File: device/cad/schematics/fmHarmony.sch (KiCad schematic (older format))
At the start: 18 parts, among them IC1 7805

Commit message: Station Log added to web app, with text-file-based physical device updates in mind. PCB and Schematic updated
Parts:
- removed U?: Ultimate_GPS_Breakout_V3, symbol Ultimate_GPS_Breakout_V3
- removed U?: Sheaff-Monk_Programmer, symbol Sheaff-Monk_Programmer
- added C7: 100n, ~, symbol C
- added IC3: ULTIMATE_GPS_BREAKOUT_V3, symbol ULTIMATE_GPS_BREAKOUT_V3
- added IC4: SHEAFF-MONK_SERIAL_TRANSLATOR, DIL32, symbol SHEAFF-MONK_SERIAL_TRANSLATOR
- added JP3: SHEAFF-MONK_PROGRAMMER, symbol SHEAFF-MONK_PROGRAMMER
- gave numbers to parts that had none: 2
- renumbered Rres to R1, Rback to R2, Rcon to VR1
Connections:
- wire segments 76 -> 100
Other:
- note removed: "GND"
- moved on the sheet: C4, C5, C6, IC2, LCD1, R1, R2, VR1

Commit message: PCB improved.
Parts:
- renumbered JP3 to JP2
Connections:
- net labels added: JP1
- net labels removed: Vin
- wire segments 100 -> 105
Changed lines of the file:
@@
 Sheet 1 1
 Title ""
-Date "27 sep 2014"
+Date "30 sep 2014"
 Rev ""
 Comp ""
@@
 L GND #PWR?
 U 1 1 5417678B
-P 8700 2100
-F 0 "#PWR?" H 8700 2100 30  0001 C CNN
-F 1 "GND" H 8700 2030 30  0001 C CNN
-F 2 "" H 8700 2100 60  0000 C CNN
-F 3 "" H 8700 2100 60  0000 C CNN
-	1    8700 2100
+P 8200 2100
+F 0 "#PWR?" H 8200 2100 30  0001 C CNN
+F 1 "GND" H 8200 2030 30  0001 C CNN
+F 2 "" H 8200 2100 60  0000 C CNN
+F 3 "" H 8200 2100 60  0000 C CNN
+	1    8200 2100
 	1    0    0    -1
 $EndComp
@@
 L VCC #PWR?
 U 1 1 5417679F
-P 8200 1900
-F 0 "#PWR?" H 8200 2000 30  0001 C CNN
-F 1 "VCC" H 8200 2000 30  0000 C CNN
-F 2 "" H 8200 1900 60  0000 C CNN
-F 3 "" H 8200 1900 60  0000 C CNN
-	1    8200 1900
+P 8700 1900
+F 0 "#PWR?" H 8700 2000 30  0001 C CNN
+F 1 "VCC" H 8700 2000 30  0000 C CNN
+F 2 "" H 8700 1900 60  0000 C CNN
+F 3 "" H 8700 1900 60  0000 C CNN
+	1    8700 1900
 	1    0    0    -1
 $EndComp
@@
 $EndComp
 Text GLabel 950  1350 0    60   Input ~ 0
-Vin
+JP1
 $Comp
 L GND #PWR?
@@
 $EndComp
 $Comp
-L SHEAFF-MONK_PROGRAMMER JP3
+L SHEAFF-MONK_PROGRAMMER JP2
 U 1 1 5426FD03
 P 4600 4600
-F 0 "JP3" V 4200 4950 60  0000 C CNN
+F 0 "JP2" V 4200 4950 60  0000 C CNN
 F 1 "SHEAFF-MONK_PROGRAMMER" H 4650 4500 60  0000 C CNN
 F 2 "" H 4650 4500 60  0000 C CNN
@@
 	9100 2400 8950 2400
 Wire Wire Line
-	8200 2000 8200 1900
-Wire Wire Line
-	8700 2000 8700 2100
+	8700 2000 8700 1900
+Wire Wire Line
+	8200 2000 8200 2100
 Wire Wire Line
 	6250 3900 5800 3900
@@
 Wire Wire Line
 	5900 4100 6250 4100
+$Comp
+L GND #PWR?
+U 1 1 5428D3A8
+P 8350 3550
+F 0 "#PWR?" H 8350 3550 30  0001 C CNN
+F 1 "GND" H 8350 3480 30  0001 C CNN
+F 2 "" H 8350 3550 60  0000 C CNN
+F 3 "" H 8350 3550 60  0000 C CNN
+	1    8350 3550
+	1    0    0    -1
+$EndComp
+Wire Wire Line
+	8250 3500 8350 3500
+Wire Wire Line
+	8350 3500 8350 3550
+Wire Wire Line
+	8250 3600 8300 3600
+Wire Wire Line
+	8300 3600 8300 3650
+Wire Wire Line
+	8300 3650 8450 3650
+Connection ~ 8450 3650
 $EndSCHEMATC

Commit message: PCB Updated to include jumper for separate car/update power sources
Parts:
- added JP4: JUMPER3, ~, symbol JUMPER3
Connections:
- wire segments 105 -> 113
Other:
- note added: "Car"
- note added: "Update"
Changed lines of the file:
@@
 Sheet 1 1
 Title ""
-Date "30 sep 2014"
+Date "1 oct 2014"
 Rev ""
 Comp ""
@@
 L VCC #PWR?
 U 1 1 5424B3C1
-P 5600 1150
-F 0 "#PWR?" H 5600 1250 30  0001 C CNN
-F 1 "VCC" H 5600 1250 30  0000 C CNN
-F 2 "" H 5600 1150 60  0000 C CNN
-F 3 "" H 5600 1150 60  0000 C CNN
-	1    5600 1150
+P 6650 1400
+F 0 "#PWR?" H 6650 1500 30  0001 C CNN
+F 1 "VCC" H 6650 1500 30  0000 C CNN
+F 2 "" H 6650 1400 60  0000 C CNN
+F 3 "" H 6650 1400 60  0000 C CNN
+	1    6650 1400
 	1    0    0    -1
 $EndComp
@@
 	1    0    0    -1
 $EndComp
-Text Notes 5700 1150 0    60   ~ 0
+Text Notes 6750 1400 0    60   ~ 0
 +5V\n
-$Comp
-L SHEAFF-MONK_SERIAL_TRANSLATOR IC4
-U 1 1 5426F555
-P 7200 7100
-F 0 "IC4" H 6400 9030 40  0000 L BNN
-F 1 "SHEAFF-MONK_SERIAL_TRANSLATOR" H 7100 6950 40  0000 L BNN
-F 2 "DIL32" H 7250 7200 30  0000 C CIN
-F 3 "" H 7250 7200 60  0000 C CNN
-	1    7200 7100
-	1    0    0    -1
-$EndComp
-$Comp
-L VCC #PWR?
-U 1 1 5426F80A
-P 5750 5500
-F 0 "#PWR?" H 5750 5600 30  0001 C CNN
-F 1 "VCC" H 5750 5600 30  0000 C CNN
-F 2 "" H 5750 5500 60  0000 C CNN
-F 3 "" H 5750 5500 60  0000 C CNN
-	1    5750 5500
-	1    0    0    -1
-$EndComp
 $Comp
 L GND #PWR?
@@
 Connection ~ 4000 1900
 Wire Wire Line
-	5100 1350 5600 1350
+	5100 1350 6200 1350
 Wire Wire Line
 	5250 1350 5250 1400
-Wire Wire Line
-	5600 1350 5600 1150
 Connection ~ 5250 1350
 Wire Wire Line
@@
 	8300 3650 8450 3650
 Connection ~ 8450 3650
+$Comp
+L JUMPER3 JP4
+U 1 1 542C4C4B
+P 6450 1050
+F 0 "JP4" H 6500 950 40  0000 L CNN
+F 1 "JUMPER3" H 6450 1150 40  0000 C CNN
+F 2 "~" H 6450 1050 60  0000 C CNN
+F 3 "~" H 6450 1050 60  0000 C CNN
+	1    6450 1050
+	1    0    0    -1
+$EndComp
+Wire Wire Line
+	6450 1150 6450 1400
+Wire Wire Line
+	6450 1400 6650 1400
+Wire Wire Line
+	6200 1350 6200 1050
+$Comp
+L SHEAFF-MONK_SERIAL_TRANSLATOR IC4
+U 1 1 5426F555
+P 7200 7100
+F 0 "IC4" H 6400 9030 40  0000 L BNN
+F 1 "SHEAFF-MONK_SERIAL_TRANSLATOR" H 7100 6950 40  0000 L BNN
+F 2 "DIL32" H 7250 7200 30  0000 C CIN
+F 3 "" H 7250 7200 60  0000 C CNN
+	1    7200 7100
+	1    0    0    -1
+$EndComp
+Wire Wire Line
+	5750 5500 5750 5300
+Wire Wire Line
+	5750 5300 6200 5300
+Wire Wire Line
+	6200 5300 6200 5100
+Wire Wire Line
+	6200 5100 10200 5100
+Wire Wire Line
+	10200 5100 10200 1050
+Wire Wire Line
+	10200 1050 6700 1050
+Text Notes 6050 950  0    60   ~ 0
+Car
+Text Notes 6700 950  0    60   ~ 0
+Update
 $EndSCHEMATC

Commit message: improved PCB and schematic. PCB sent in for fabrication Mk1
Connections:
- wire segments 113 -> 117
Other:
- note added: "JP3\n"
- moved on the sheet: C3
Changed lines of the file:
@@
 Sheet 1 1
 Title ""
-Date "1 oct 2014"
+Date "5 oct 2014"
 Rev ""
 Comp ""
@@
 L CP1 C3
 U 1 1 5424AA5D
-P 5250 1600
-F 0 "C3" H 5300 1700 50  0000 L CNN
-F 1 "1u" H 5300 1500 50  0000 L CNN
-F 2 "~" H 5250 1600 60  0000 C CNN
-F 3 "~" H 5250 1600 60  0000 C CNN
-	1    5250 1600
+P 6450 1600
+F 0 "C3" H 6500 1700 50  0000 L CNN
+F 1 "1u" H 6500 1500 50  0000 L CNN
+F 2 "~" H 6450 1600 60  0000 C CNN
+F 3 "~" H 6450 1600 60  0000 C CNN
+	1    6450 1600
 	1    0    0    -1
 $EndComp
@@
 Wire Wire Line
 	4400 1350 4600 1350
-Wire Wire Line
-	5250 1900 5250 1800
 Connection ~ 4000 1900
 Wire Wire Line
 	5100 1350 6200 1350
-Wire Wire Line
-	5250 1350 5250 1400
 Connection ~ 5250 1350
 Wire Wire Line
@@
 Text Notes 6700 950  0    60   ~ 0
 Update
+$Comp
+L GND #PWR?
+U 1 1 54316390
+P 6450 2000
+F 0 "#PWR?" H 6450 2000 30  0001 C CNN
+F 1 "GND" H 6450 1930 30  0001 C CNN
+F 2 "" H 6450 2000 60  0000 C CNN
+F 3 "" H 6450 2000 60  0000 C CNN
+	1    6450 2000
+	1    0    0    -1
+$EndComp
+Wire Wire Line
+	6450 1800 6450 2000
+Wire Wire Line
+	5700 2600 6250 2600
+Wire Wire Line
+	6250 2700 5700 2700
+Wire Wire Line
+	6250 2800 5700 2800
+Wire Wire Line
+	6250 2900 5700 2900
+Wire Wire Line
+	6250 3000 5700 3000
+Text Notes 5650 2850 1    60   ~ 0
+JP3\n
 $EndSCHEMATC

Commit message: updated project schematic
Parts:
- added LED1, LED2, LED3: (no value), ~, symbol LED
- added R3, R4, R5: 100, symbol R
- added SW1: (no value), ~, symbol SW_PUSH
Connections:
- wire segments 117 -> 131
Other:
- note removed: "JP3\n"

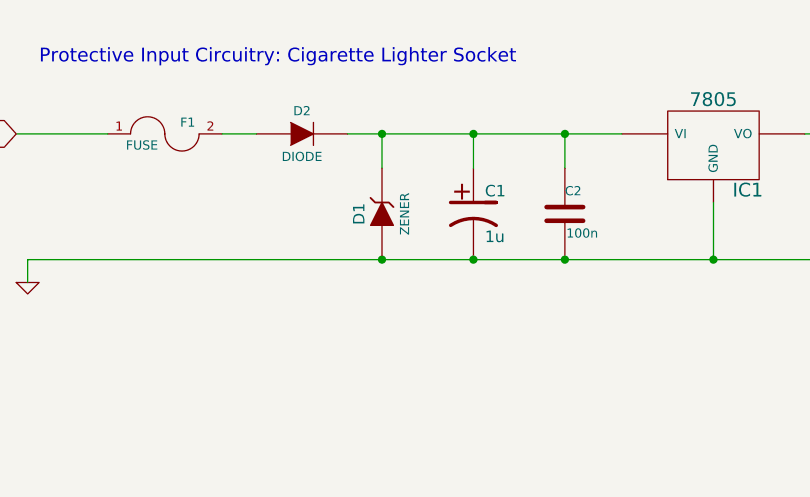
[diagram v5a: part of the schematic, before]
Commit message: The Big Genre Filtering Update! Python used to crawl Wikipedias official national FM stations listing. Genres are parsed out, associatively matched with our genre keywords, and the FM Stations PostgreSQL database is updated accordingly.
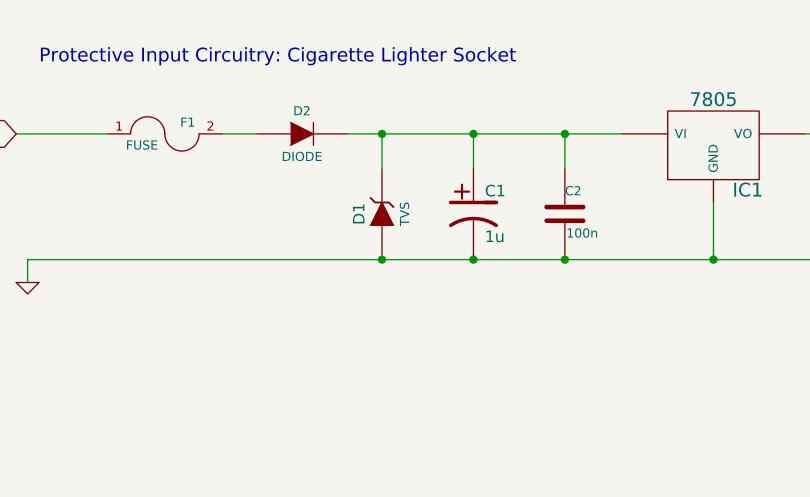
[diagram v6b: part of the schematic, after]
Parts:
- D1: value ZENER -> TVS
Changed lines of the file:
@@
 Sheet 1 1
 Title ""
-Date "3 nov 2014"
+Date "1 dec 2014"
 Rev ""
 Comp ""
@@
 P 2550 1700
 F 0 "D1" H 2550 1800 50  0000 C CNN
-F 1 "ZENER" H 2550 1600 40  0000 C CNN
+F 1 "TVS" H 2550 1600 40  0000 C CNN
 F 2 "~" H 2550 1700 60  0000 C CNN
 F 3 "~" H 2550 1700 60  0000 C CNN

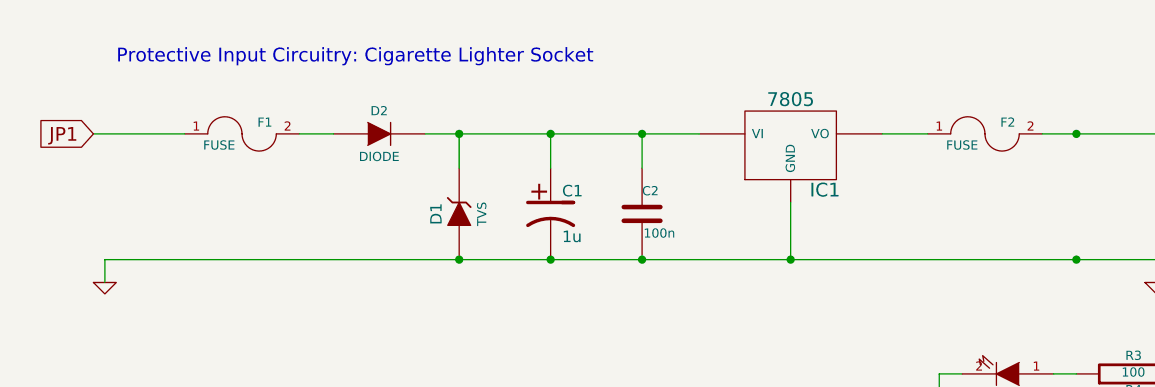
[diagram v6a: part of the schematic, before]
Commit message: cleaned up source code and improved schematic.
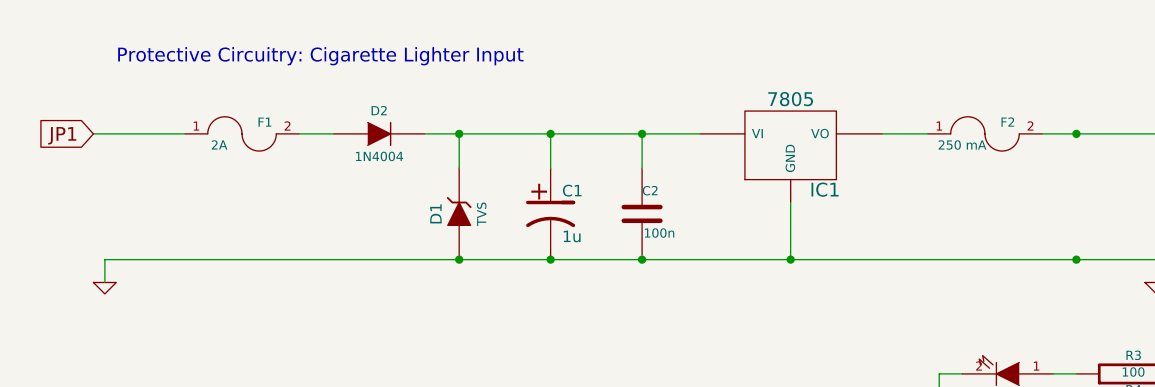
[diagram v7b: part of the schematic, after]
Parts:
- D2: value DIODE -> 1N4004
- F1: value FUSE -> 2A
- F2: value FUSE -> 250 mA
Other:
- note added: "Protective Circuitry: Cigarette Lighter Input"
- note removed: "Protective Input Circuitry: Cigarette Lighter Socket"
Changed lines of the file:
@@
 Sheet 1 1
 Title ""
-Date "1 dec 2014"
+Date "13 dec 2014"
 Rev ""
 Comp ""
@@
 P 2200 1350
 F 0 "D2" H 2200 1450 40  0000 C CNN
-F 1 "DIODE" H 2200 1250 40  0000 C CNN
+F 1 "1N4004" H 2200 1250 40  0000 C CNN
 F 2 "~" H 2200 1350 60  0000 C CNN
 F 3 "~" H 2200 1350 60  0000 C CNN
@@
 P 1600 1350
 F 0 "F1" H 1700 1400 40  0000 C CNN
-F 1 "FUSE" H 1500 1300 40  0000 C CNN
+F 1 "2A" H 1500 1300 40  0000 C CNN
 F 2 "~" H 1600 1350 60  0000 C CNN
 F 3 "~" H 1600 1350 60  0000 C CNN
@@
 P 4850 1350
 F 0 "F2" H 4950 1400 40  0000 C CNN
-F 1 "FUSE" H 4750 1300 40  0000 C CNN
+F 1 "250 mA" H 4750 1300 40  0000 C CNN
 F 2 "~" H 4850 1350 60  0000 C CNN
 F 3 "~" H 4850 1350 60  0000 C CNN
@@
 $EndComp
 Text Notes 1050 1050 0    60   ~ 0
-Protective Input Circuitry: Cigarette Lighter Socket
+Protective Circuitry: Cigarette Lighter Input
 $Comp
 L C C4
